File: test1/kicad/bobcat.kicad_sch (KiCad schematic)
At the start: 24 parts, among them U20 Bobcat

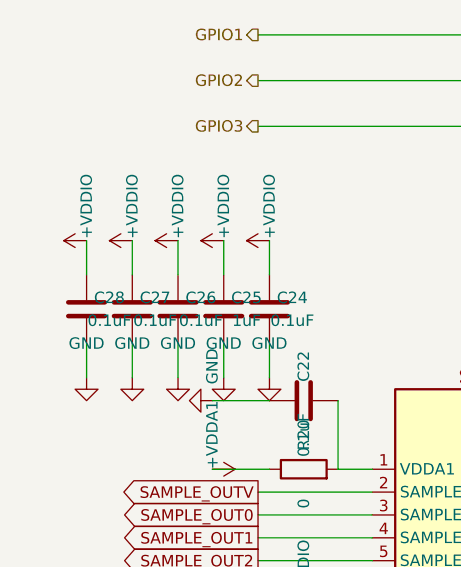
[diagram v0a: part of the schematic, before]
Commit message: Close 5 of 6 review findings: Bobcat symbol pin types + C29 VDDIO cap
Applied corrections for all actionable findings from the second
pipeline run (c19f6f9).

E1-E3 — Bobcat symbol OSC_EN/WEIGHT_EN/SAMPLE_TRIG (pins 23/24/25):
  pin type input → output. The chip drives these outputs (per Bobcat
  PDF page 4 "Signal outputs"); the symbol's old `input` declaration
  contradicted the DUT spec.

E4 — Bobcat symbol BIAS0/BIAS1 (pins 28/29):
  pin type passive → input. Current is sourced INTO these pins by the
  PMOS pass elements (V-to-I bias topology); `passive` obscured the
  electrical intent. `input` makes the current-sink role explicit and
  matches the netlist's direction=input declaration.

W1 — Bobcat +VDDIO decoupling 5/6 caps:
  Added C29 = 0.1µF as the 5th per-pin cap (matching the original
  W2 resolution intent of 5×0.1µF per-pin + 1×1µF bulk). Extended
  the VDDIO_ROW loop in build_bobcat.py to include C29.

W2 — MCP4728 VREF + EEPROM provisioning remains as a WARNING.
  This is an assembly-time gotcha (already documented in
  design_requirements.md line 91); no schematic-level fix possible.
  Leaving it surfaced each run as a recurring reminder until we
  decide whether to add an acknowledged-warning suppression mechanism.

Final state:
  Before: 4 ERRORs · 2 WARNINGs · 0 INFOs
  After:  0 ERRORs · 1 WARNING  · 0 INFOs  (the W2 reminder)

Build still clean: 0 ERROR, 17 WARNING, 12 INFO (1 extra INFO is
a redundant_junction at C29 — pre-existing pattern, not new).

Co-Authored-By: Claude Opus 4.7 <noreply@anthropic.com>
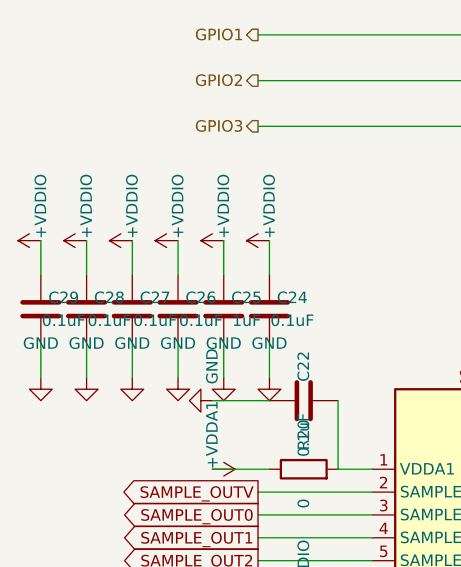
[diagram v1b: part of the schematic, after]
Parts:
- added C29: 0.1uF, Capacitor_SMD:C_0402_1005Metric, symbol Device:C
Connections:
- net +VDDIO: now also C29.1
- net GND: now also C29.2
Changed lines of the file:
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@@
       (project "test1"
         (path "/4ed7a046-ef33-57d9-8730-321c05965af3/e6b90fa2-2dfc-5319-a99a-2ebf8a1933a0" (reference "#PWRa20f2c5c") (unit 1)))))
+  (symbol
+    (lib_id "Device:C")
+    (at 139.7 100.33 0)
+    (unit 1) (in_bom yes) (on_board yes) (dnp no)
+    (property "Reference" "C29" (at 142.24 99.06 0) (effects (font (size 1.27 1.27))))
+    (property "Value" "0.1uF" (at 142.24 101.6 0) (effects (font (size 1.27 1.27))))
+    (property "Footprint" "Capacitor_SMD:C_0402_1005Metric" (at 0 0 0) (effects (font (size 1.27 1.27)) (hide yes)))
+    (property "Datasheet" "" (at 0 0 0) (effects (font (size 1.27 1.27)) (hide yes)))
+    (pin "1")
+    (pin "2")
+    (instances
+      (project "test1"
+        (path "/4ed7a046-ef33-57d9-8730-321c05965af3/e6b90fa2-2dfc-5319-a99a-2ebf8a1933a0" (reference "C29") (unit 1)))))
+  (wire (pts (xy 139.7 96.52) (xy 139.7 92.71)) (stroke (width 0) (type default)))
+  (symbol
+    (lib_id "power:+VDDIO")
+    (at 139.7 92.71 90)
+    (unit 1) (in_bom yes) (on_board yes) (dnp no)
+    (property "Reference" "#PWR37b362c0" (at 139.7 86.36 0) (effects (font (size 1.27 1.27)) (hide yes)))
+    (property "Value" "+VDDIO" (at 139.7 88.9 0) (effects (font (size 1.27 1.27))))
+    (property "Footprint" "" (at 0 0 0) (effects (font (size 1.27 1.27)) (hide yes)))
+    (property "Datasheet" "" (at 0 0 0) (effects (font (size 1.27 1.27)) (hide yes)))
+    (pin "1")
+    (instances
+      (project "test1"
+        (path "/4ed7a046-ef33-57d9-8730-321c05965af3/e6b90fa2-2dfc-5319-a99a-2ebf8a1933a0" (reference "#PWR37b362c0") (unit 1)))))
+  (wire (pts (xy 139.7 104.14) (xy 139.7 107.95)) (stroke (width 0) (type default)))
+  (symbol
+    (lib_id "power:GND")
+    (at 139.7 107.95 0)
+    (unit 1) (in_bom yes) (on_board yes) (dnp no)
+    (property "Reference" "#PWR2794fcca" (at 139.7 101.6 0) (effects (font (size 1.27 1.27)) (hide yes)))
+    (property "Value" "GND" (at 139.7 104.14 0) (effects (font (size 1.27 1.27))))
+    (property "Footprint" "" (at 0 0 0) (effects (font (size 1.27 1.27)) (hide yes)))
+    (property "Datasheet" "" (at 0 0 0) (effects (font (size 1.27 1.27)) (hide yes)))
+    (pin "1")
+    (instances
+      (project "test1"
+        (path "/4ed7a046-ef33-57d9-8730-321c05965af3/e6b90fa2-2dfc-5319-a99a-2ebf8a1933a0" (reference "#PWR2794fcca") (unit 1)))))
   (wire (pts (xy 195.58 152.4) (xy 195.58 185.42)) (stroke (width 0) (type default)))
   (wire (pts (xy 195.58 185.42) (xy 165.1 185.42)) (stroke (width 0) (type default)))
